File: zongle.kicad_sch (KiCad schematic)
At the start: 21 parts, among them U1 453-00059R

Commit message: removed usb testpoints
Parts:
- removed TpD+1: D+, TestPoint:TestPoint_Pad_1.0x1.0mm, symbol Connector:TestPoint
- removed TpD-1: D-, TestPoint:TestPoint_Pad_1.0x1.0mm, symbol Connector:TestPoint
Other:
- moved on the sheet: TpVBUS1
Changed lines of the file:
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@@
 		)
 	)
-	(global_label "D+"
-		(shape input)
-		(at 53.34 46.99 270)
-		(fields_autoplaced yes)
-		(effects
-			(font
-				(size 1.27 1.27)
-			)
-			(justify right)
-		)
-		(property "Intersheetrefs" "${INTERSHEET_REFS}"
-			(at 53.34 52.8176 90)
-			(effects
-				(font
-					(size 1.27 1.27)
-				)
-				(justify right)
-				(hide yes)
-			)
-		)
-	)
 	(global_label "LED_ST"
 		(shape input)
@@
 		)
 	)
-	(global_label "D-"
-		(shape input)
-		(at 67.31 46.99 270)
-		(fields_autoplaced yes)
-		(effects
-			(font
-				(size 1.27 1.27)
-			)
-			(justify right)
-		)
-		(property "Intersheetrefs" "${INTERSHEET_REFS}"
-			(at 67.31 52.8176 90)
-			(effects
-				(font
-					(size 1.27 1.27)
-				)
-				(justify right)
-				(hide yes)
-			)
-		)
-	)
 	(global_label "SWDIO"
 		(shape input)
@@
 	(global_label "VBUS_Raw"
 		(shape input)
-		(at 25.4 25.4 270)
+		(at 53.34 46.99 270)
 		(fields_autoplaced yes)
 		(effects
@@
 		)
 		(property "Intersheetrefs" "${INTERSHEET_REFS}"
-			(at 25.4 38.0009 90)
+			(at 53.34 59.5909 90)
 			(effects
 				(font
@@
 	(symbol
 		(lib_id "Connector:TestPoint")
-		(at 67.31 46.99 0)
-		(unit 1)
-		(exclude_from_sim no)
-		(in_bom yes)
-		(on_board yes)
-		(dnp no)
-		(fields_autoplaced yes)
-		(property "Reference" "TpD-1"
-			(at 69.85 42.4179 0)
-			(effects
-				(font
-					(size 1.27 1.27)
-				)
-				(justify left)
-			)
-		)
-		(property "Value" "D-"
-			(at 69.85 44.9579 0)
-			(effects
-				(font
-					(size 1.27 1.27)
-				)
-				(justify left)
-			)
-		)
-		(property "Footprint" "TestPoint:TestPoint_Pad_1.0x1.0mm"
-			(at 72.39 46.99 0)
-			(effects
-				(font
-					(size 1.27 1.27)
-				)
-				(hide yes)
-			)
-		)
-		(property "Datasheet" "~"
-			(at 72.39 46.99 0)
-			(effects
-				(font
-					(size 1.27 1.27)
-				)
-				(hide yes)
-			)
-		)
-		(property "Description" "test point"
-			(at 67.31 46.99 0)
-			(effects
-				(font
-					(size 1.27 1.27)
-				)
-				(hide yes)
-			)
-		)
-		(pin "1"
-		)
-		(instances
-			(project "zongle"
-				(path "/e563ac8d-b93c-431b-8d13-48f254367838"
-					(reference "TpD-1")
-					(unit 1)
-				)
-			)
-		)
-	)
-	(symbol
-		(lib_id "Connector:TestPoint")
 		(at 39.37 46.99 0)
 		(unit 1)
@@
 	)
 	(symbol
-		(lib_id "Connector:TestPoint")
-		(at 53.34 46.99 0)
-		(unit 1)
-		(exclude_from_sim no)
-		(in_bom yes)
-		(on_board yes)
-		(dnp no)
-		(fields_autoplaced yes)
-		(property "Reference" "TpD+1"
-			(at 55.88 42.4179 0)
-			(effects
-				(font
-					(size 1.27 1.27)
-				)
-				(justify left)
-			)
-		)
-		(property "Value" "D+"
-			(at 55.88 44.9579 0)
-			(effects
-				(font
-					(size 1.27 1.27)
-				)
-				(justify left)
-			)
-		)
-		(property "Footprint" "TestPoint:TestPoint_Pad_1.0x1.0mm"
-			(at 58.42 46.99 0)
-			(effects
-				(font
-					(size 1.27 1.27)
-				)
-				(hide yes)
-			)
-		)
-		(property "Datasheet" "~"
-			(at 58.42 46.99 0)
-			(effects
-				(font
-					(size 1.27 1.27)
-				)
-				(hide yes)
-			)
-		)
-		(property "Description" "test point"
-			(at 53.34 46.99 0)
-			(effects
-				(font
-					(size 1.27 1.27)
-				)
-				(hide yes)
-			)
-		)
-		(pin "1"
-		)
-		(instances
-			(project "zongle"
-				(path "/e563ac8d-b93c-431b-8d13-48f254367838"
-					(reference "TpD+1")
-					(unit 1)
-				)
-			)
-		)
-	)
-	(symbol
 		(lib_id "power:+5V")
 		(at 175.26 74.93 0)
@@
 	(symbol
 		(lib_id "Connector:TestPoint")
-		(at 25.4 25.4 0)
+		(at 53.34 46.99 0)
 		(unit 1)
 		(exclude_from_sim no)
@@
 		(fields_autoplaced yes)
 		(property "Reference" "TpVBUS1"
-			(at 27.94 20.8279 0)
+			(at 55.88 42.4179 0)
 			(effects
 				(font
@@
 		)
 		(property "Value" "VBUS"
-			(at 27.94 23.3679 0)
+			(at 55.88 44.9579 0)
 			(effects
 				(font
@@
 		)
 		(property "Footprint" "TestPoint:TestPoint_Pad_1.0x1.0mm"
-			(at 30.48 25.4 0)
+			(at 58.42 46.99 0)
 			(effects
 				(font
@@
 		)
 		(property "Datasheet" "~"
-			(at 30.48 25.4 0)
+			(at 58.42 46.99 0)
 			(effects
 				(font
@@
 		)
 		(property "Description" "test point"
-			(at 25.4 25.4 0)
+			(at 53.34 46.99 0)
 			(effects
 				(font

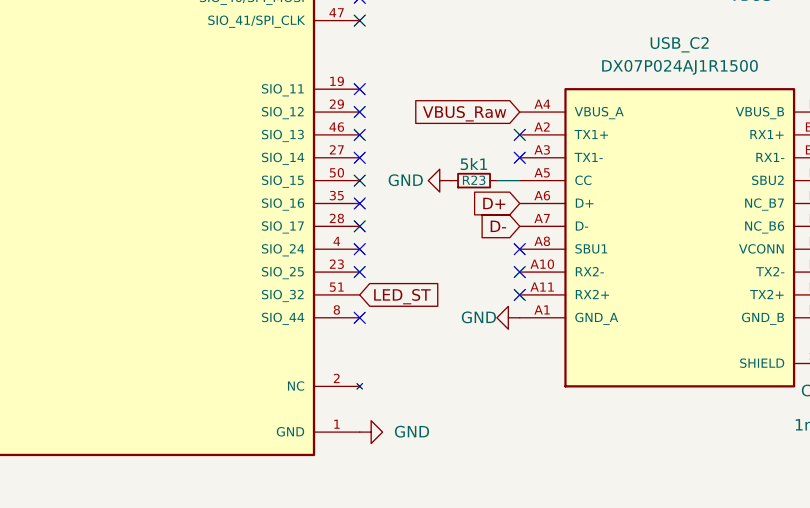
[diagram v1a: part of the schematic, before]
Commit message: cleaned usb traces. moved esd closer to usb
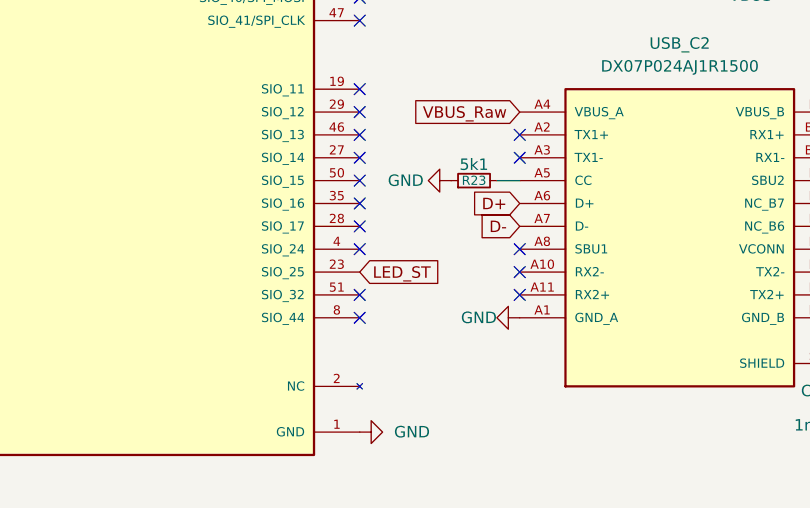
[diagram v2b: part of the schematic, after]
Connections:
- net LED_ST: now also U1.23 (SIO_25); no longer U1.51 (SIO_32)
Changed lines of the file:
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@@
-	)
-	(no_connect
-		(at 132.08 110.49)
 	)
 	(no_connect
@@
 	(no_connect
 		(at 71.12 77.47)
+	)
+	(no_connect
+		(at 132.08 113.03)
 	)
 	(no_connect
@@
 	(global_label "LED_ST"
 		(shape input)
-		(at 132.08 113.03 0)
+		(at 132.08 110.49 0)
 		(fields_autoplaced yes)
 		(effects
@@
 		)
 		(property "Intersheetrefs" "${INTERSHEET_REFS}"
-			(at 141.657 113.03 0)
+			(at 141.657 110.49 0)
 			(effects
 				(font

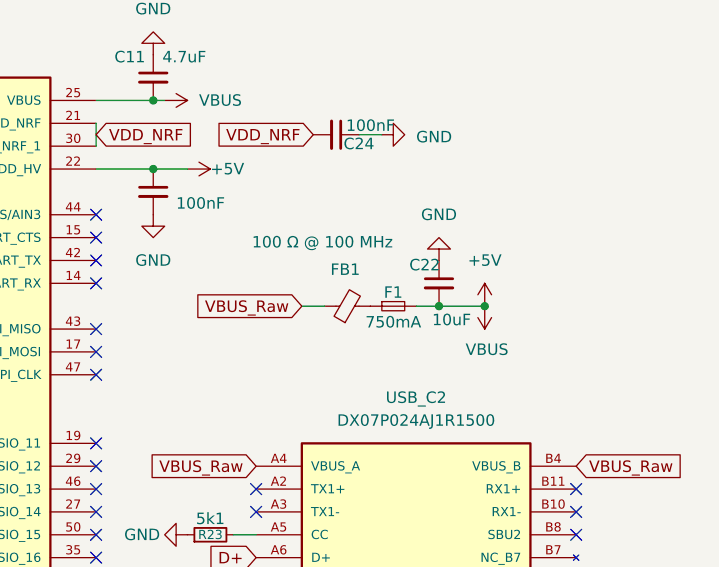
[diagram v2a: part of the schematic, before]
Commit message: some routing refinements. moved all components as far away from the antenna as possible. added another decup cap to the power path. changed board thickness to 0.8mm to accomodate for usb-c plug. some layout optimizations
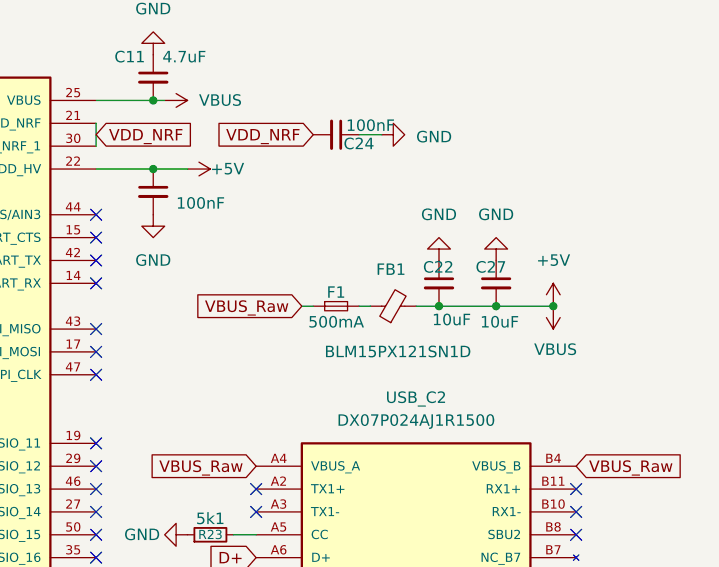
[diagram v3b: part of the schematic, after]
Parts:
- added C27: 10uF, Capacitor_SMD:C_0402_1005Metric, symbol Device:C_Small
- F1: value 750mA -> 500mA
- FB1: value 100 Ω @ 100 MHz -> BLM15PX121SN1D
- R21, R23, R26: footprint Resistor_SMD:R_0402_1005Metric -> Resistor_SMD:R_0201_0603Metric
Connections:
- net +5V: now also FB1.2, C27.2; no longer F1.2
- net GND: now also C27.1
- net VBUS_A: now also F1.1; no longer FB1.1
- new net: F1.2, FB1.1
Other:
- moved on the sheet: F1, FB1
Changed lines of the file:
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@@
 	)
 	(junction
+		(at 176.53 74.93)
+		(diameter 0)
+		(color 0 0 0 0)
+	)
+	(junction
 		(at 185.42 123.19)
 		(diameter 0)
@@
 	)
 	(junction
-		(at 175.26 74.93)
+		(at 182.88 74.93)
 		(diameter 0)
 		(color 0 0 0 0)
@@
 	(wire
 		(pts
+			(xy 161.29 74.93) (xy 162.56 74.93)
+		)
+		(stroke
+			(width 0)
+			(type default)
+		)
+	)
+	(wire
+		(pts
 			(xy 147.32 100.33) (xy 149.86 100.33)
 		)
@@
 	(wire
 		(pts
+			(xy 176.53 74.93) (xy 182.88 74.93)
+		)
+		(stroke
+			(width 0)
+			(type default)
+		)
+	)
+	(wire
+		(pts
 			(xy 132.08 52.07) (xy 138.43 52.07)
 		)
@@
 	(wire
 		(pts
-			(xy 170.18 74.93) (xy 175.26 74.93)
+			(xy 156.21 74.93) (xy 154.94 74.93)
 		)
 		(stroke
@@
 	(wire
 		(pts
-			(xy 132.08 59.69) (xy 138.43 59.69)
+			(xy 170.18 74.93) (xy 176.53 74.93)
 		)
 		(stroke
@@
 	(wire
 		(pts
-			(xy 184.15 123.19) (xy 185.42 123.19)
+			(xy 132.08 59.69) (xy 138.43 59.69)
 		)
 		(stroke
@@
 	(wire
 		(pts
-			(xy 167.64 74.93) (xy 170.18 74.93)
+			(xy 184.15 123.19) (xy 185.42 123.19)
 		)
 		(stroke
@@
 	(wire
 		(pts
-			(xy 138.43 59.69) (xy 142.24 59.69)
+			(xy 167.64 74.93) (xy 170.18 74.93)
 		)
 		(stroke
@@
 	(wire
 		(pts
-			(xy 185.42 123.19) (xy 187.96 123.19)
+			(xy 138.43 59.69) (xy 142.24 59.69)
 		)
 		(stroke
@@
 	(wire
 		(pts
-			(xy 132.08 54.61) (xy 132.08 57.15)
+			(xy 185.42 123.19) (xy 187.96 123.19)
 		)
 		(stroke
@@
 	(wire
 		(pts
-			(xy 154.94 74.93) (xy 157.48 74.93)
+			(xy 132.08 54.61) (xy 132.08 57.15)
 		)
 		(stroke
@@
 		(dnp no)
 		(property "Reference" "C22"
-			(at 166.878 70.358 0)
+			(at 168.402 70.612 0)
 			(effects
 				(font
@@
 			)
 		)
-		(property "Footprint" "Resistor_SMD:R_0402_1005Metric"
+		(property "Footprint" "Resistor_SMD:R_0201_0603Metric"
 			(at 187.96 125.73 0)
 			(effects
@@
 	(symbol
 		(lib_id "power:+5V")
-		(at 175.26 74.93 0)
+		(at 182.88 74.93 0)
 		(unit 1)
 		(exclude_from_sim no)
@@
 		(fields_autoplaced yes)
 		(property "Reference" "#PWR04"
-			(at 175.26 78.74 0)
+			(at 182.88 78.74 0)
 			(effects
 				(font
@@
 		)
 		(property "Value" "+5V"
-			(at 175.26 69.85 0)
+			(at 182.88 69.85 0)
 			(effects
 				(font
@@
 		)
 		(property "Footprint" ""
-			(at 175.26 74.93 0)
+			(at 182.88 74.93 0)
 			(effects
 				(font
@@
 		)
 		(property "Datasheet" ""
-			(at 175.26 74.93 0)
+			(at 182.88 74.93 0)
 			(effects
 				(font
@@
 		)
 		(property "Description" "Power symbol creates a global label with name \"+5V\""
-			(at 175.26 74.93 0)
+			(at 182.88 74.93 0)
 			(effects
 				(font
@@
 	(symbol
 		(lib_id "Device:FerriteBead_Small")
-		(at 160.02 74.93 90)
+		(at 165.1 74.93 90)
 		(unit 1)
 		(exclude_from_sim no)
@@
 		(dnp no)
 		(property "Reference" "FB1"
-			(at 159.766 70.866 90)
+			(at 164.846 70.866 90)
 			(effects
 				(font
@@
 			)
 		)
-		(property "Value" "100 Ω @ 100 MHz"
-			(at 157.226 67.818 90)
+		(property "Value" "BLM15PX121SN1D"
+			(at 165.608 80.01 90)
 			(effects
 				(font
@@
 		)
 		(property "Footprint" "Resistor_SMD:R_0402_1005Metric"
-			(at 160.02 76.708 90)
+			(at 165.1 76.708 90)
 			(effects
 				(font
@@
 		)
 		(property "Datasheet" "~"
-			(at 160.02 74.93 0)
+			(at 165.1 74.93 0)
 			(effects
 				(font
@@
 		)
 		(property "Description" "Ferrite bead, small symbol"
-			(at 160.02 74.93 0)
+			(at 165.1 74.93 0)
 			(effects
 				(font
@@
 			)
 		)
-		(property "Footprint" "Resistor_SMD:R_0402_1005Metric"
+		(property "Footprint" "Resistor_SMD:R_0201_0603Metric"
 			(at 144.78 100.33 0)
 			(effects
@@
 			)
 		)
-		(property "Footprint" "Resistor_SMD:R_0402_1005Metric"
+		(property "Footprint" "Resistor_SMD:R_0201_0603Metric"
 			(at 97.79 38.1 0)
 			(effects
@@
 	(symbol
 		(lib_id "power:VBUS")
-		(at 175.26 74.93 180)
+		(at 182.88 74.93 180)
 		(unit 1)
 		(exclude_from_sim no)
@@
 		(dnp no)
 		(property "Reference" "#PWR018"
-			(at 175.26 71.12 0)
+			(at 182.88 71.12 0)
 			(effects
 				(font
@@
 		)
 		(property "Value" "VBUS"
-			(at 175.514 79.756 0)
+			(at 183.134 79.756 0)
 			(effects
 				(font
@@
 		)
 		(property "Footprint" ""
-			(at 175.26 74.93 0)
+			(at 182.88 74.93 0)
 			(effects
 				(font
@@
 		)
 		(property "Datasheet" ""
-			(at 175.26 74.93 0)
+			(at 182.88 74.93 0)
 			(effects
 				(font
@@
 		)
 		(property "Description" "Power symbol creates a global label with name \"VBUS\""
-			(at 175.26 74.93 0)
+			(at 182.88 74.93 0)
 			(effects
 				(font
@@
 	)
 	(symbol
+		(lib_id "Device:C_Small")
+		(at 176.53 72.39 0)
+		(unit 1)
+		(exclude_from_sim no)
+		(in_bom yes)
+		(on_board yes)
+		(dnp no)
+		(property "Reference" "C27"
+			(at 174.244 70.612 0)
+			(effects
+				(font
+					(size 1.27 1.27)
+				)
+				(justify left)
+			)
+		)
+		(property "Value" "10uF"
+			(at 174.752 76.708 0)
+			(effects
+				(font
+					(size 1.27 1.27)
+				)
+				(justify left)
+			)
+		)
+		(property "Footprint" "Capacitor_SMD:C_0402_1005Metric"
+			(at 176.53 72.39 0)
+			(effects
+				(font
+					(size 1.27 1.27)
+				)
+				(hide yes)
+			)
+		)
+		(property "Datasheet" "~"
+			(at 176.53 72.39 0)
+			(effects
+				(font
+					(size 1.27 1.27)
+				)
+				(hide yes)
+			)
+		)
+		(property "Description" "Unpolarized capacitor, small symbol"
+			(at 176.53 72.39 0)
+			(effects
+				(font
+					(size 1.27 1.27)
+				)
+				(hide yes)
+			)
+		)
+		(pin "1"
+		)
+		(pin "2"
+		)
+		(instances
+			(project "zongle"
+				(path "/e563ac8d-b93c-431b-8d13-48f254367838"
+					(reference "C27")
+					(unit 1)
+				)
+			)
+		)
+	)
+	(symbol
 		(lib_id "power:GND")
 		(at 142.24 100.33 270)
@@
 	(symbol
 		(lib_id "Device:Fuse_Small")
-		(at 165.1 74.93 0)
+		(at 158.75 74.93 0)
 		(unit 1)
 		(exclude_from_sim no)
@@
 		(dnp no)
 		(property "Reference" "F1"
-			(at 165.1 73.406 0)
+			(at 158.75 73.406 0)
 			(effects
 				(font
@@
 			)
 		)
-		(property "Value" "750mA"
-			(at 165.1 76.708 0)
+		(property "Value" "500mA"
+			(at 158.75 76.708 0)
 			(effects
 				(font
@@
 		)
 		(property "Footprint" "Fuse:Fuse_0402_1005Metric"
-			(at 165.1 74.93 0)
+			(at 158.75 74.93 0)
 			(effects
 				(font
@@
 		)
 		(property "Datasheet" "~"
-			(at 165.1 74.93 0)
+			(at 158.75 74.93 0)
 			(effects
 				(font
@@
 		)
 		(property "Description" "Fuse, small symbol"
-			(at 165.1 74.93 0)
+			(at 158.75 74.93 0)
 			(effects
 				(font
@@
 					(unit 1)
 				)
+			)
+		)
+	)
+	(symbol
+		(lib_id "power:GND")
+		(at 176.53 69.85 180)
+		(unit 1)
+		(exclude_from_sim no)
+		(in_bom yes)
+		(on_board yes)
+		(dnp no)
+		(fields_autoplaced yes)
+		(property "Reference" "#PWR01"
+			(at 176.53 63.5 0)
+			(effects
+				(font
+					(size 1.27 1.27)
+				)
+				(hide yes)
+			)
+		)
+		(property "Value" "GND"
+			(at 176.53 64.77 0)
+			(effects
+				(font
+					(size 1.27 1.27)
+				)
+			)
+		)
+		(property "Footprint" ""
+			(at 176.53 69.85 0)
+			(effects
+				(font
+					(size 1.27 1.27)
+				)
+				(hide yes)
+			)
+		)
+		(property "Datasheet" ""
+			(at 176.53 69.85 0)
+			(effects
+				(font
+					(size 1.27 1.27)
+				)
+				(hide yes)
+			)
+		)
+		(property "Description" "Power symbol creates a global label with name \"GND\" , ground"
+			(at 176.53 69.85 0)
+			(effects
+				(font
+					(size 1.27 1.27)
+				)
+				(hide yes)
+			)
+		)
+		(pin "1"
+		)
+		(instances
+			(project "zongle"
+				(path "/e563ac8d-b93c-431b-8d13-48f254367838"
+					(reference "#PWR01")
+					(unit 1)
+				)
